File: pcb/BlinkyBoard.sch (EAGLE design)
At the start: 17 parts, among them Q1 16 MHz

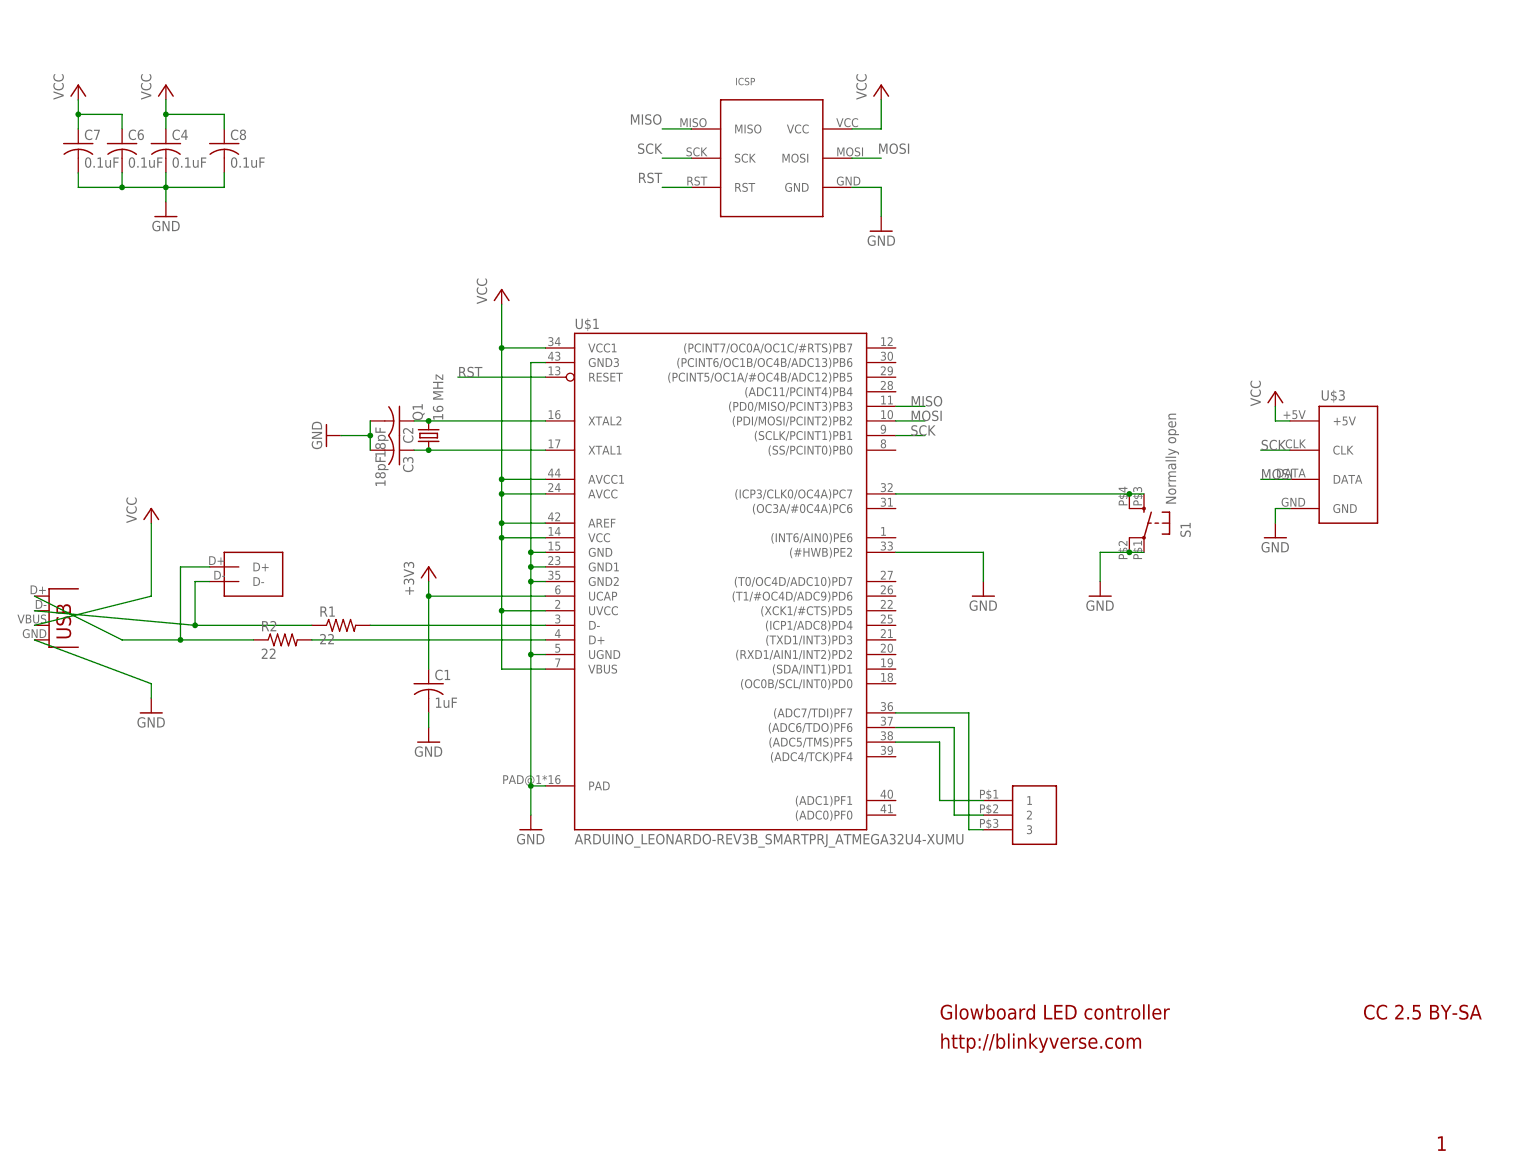
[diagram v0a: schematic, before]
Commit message: Switch to 2520 crystal, remove unused layers, rename components
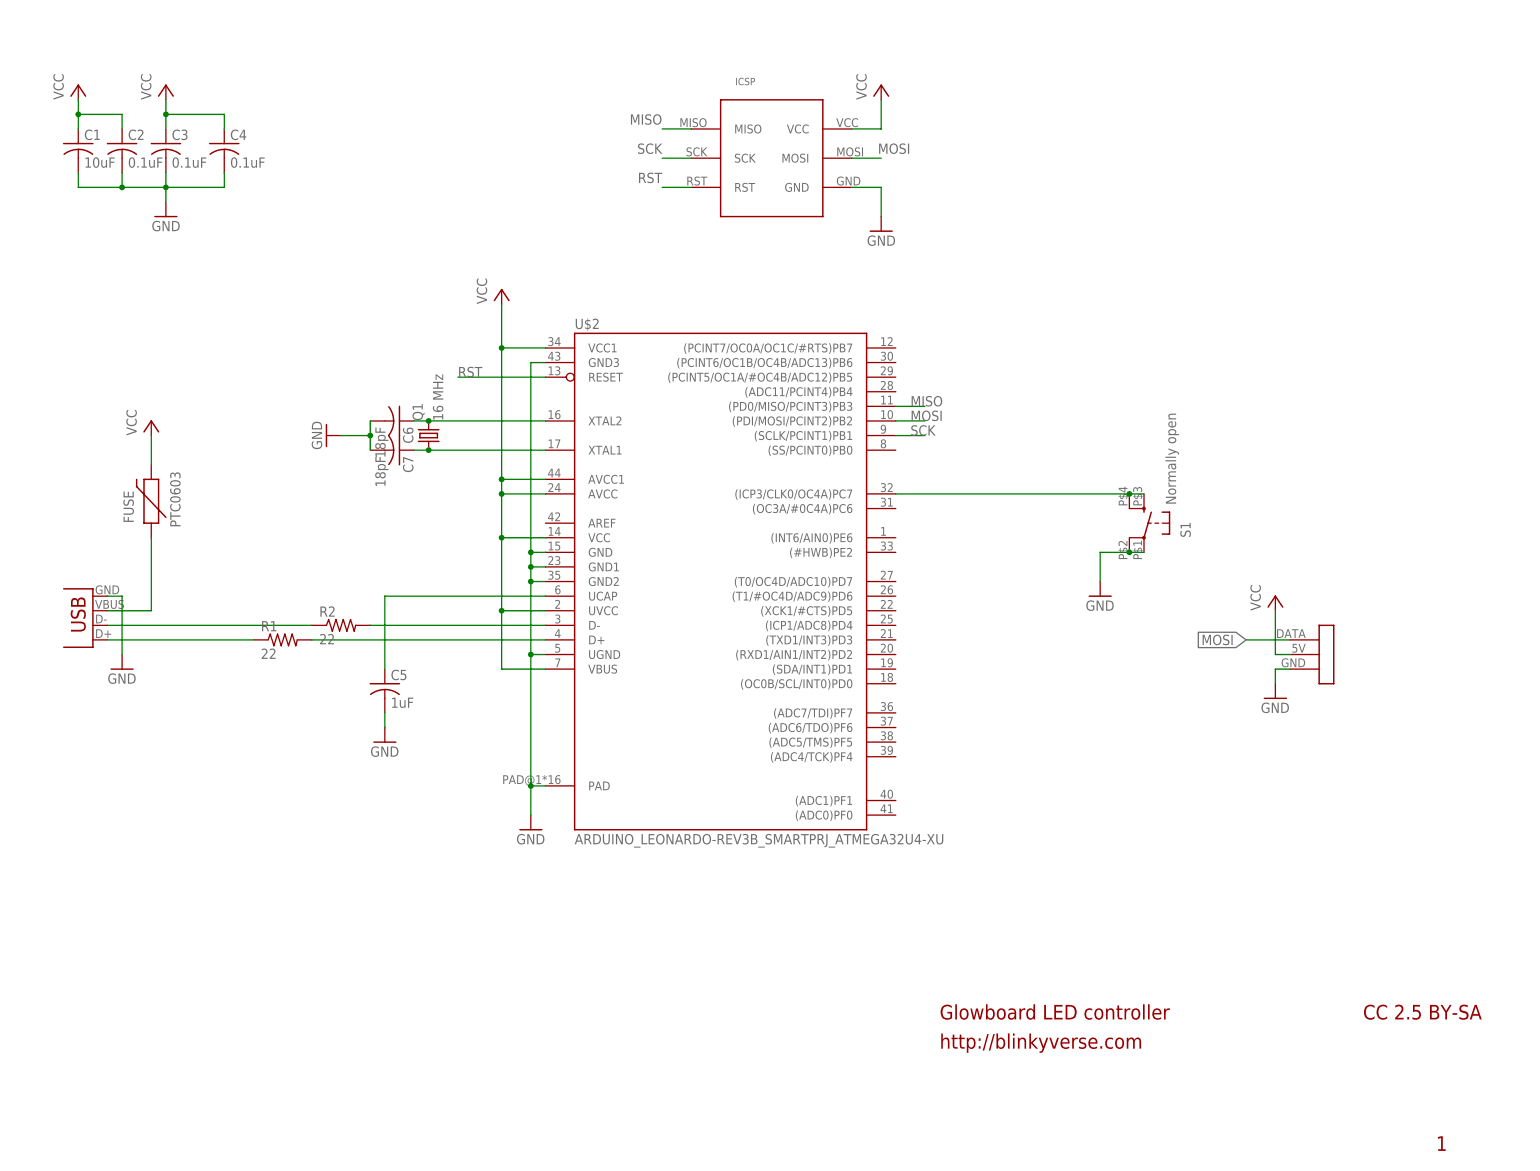
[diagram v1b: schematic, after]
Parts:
- removed C8: 0.1uF, adafruit:C-USC0603
- removed U$4: GLOWBOARD_ICSP, blinkyboard:GLOWBOARD_ICSP
- removed U$5: GLOWBOARD_EXPANSION_HEADER, blinkyboard:GLOWBOARD_EXPANSION_HEADER
- removed U$6: USB-MICROB, SparkFun:USB-MICROB
- added C5: 1uF, adafruit:C-USC0402
- added FUSE: PTC0603, SparkFun-PowerIC:PTC0603
- added WS1: WS2811_CONNECTOR, blinkiverse:WS2811_CONNECTOR
- C1: value 1uF -> 10uF; device adafruit:C-USC0603 -> adafruit:C-USC0402
- C2, C3: value 18pF -> 0.1uF; device adafruit:C-USC0603 -> adafruit:C-USC0402
- C4: device adafruit:C-USC0603 -> adafruit:C-USC0402
- C6, C7: value 0.1uF -> 18pF; device adafruit:C-USC0603 -> adafruit:C-USC0402
- Q1: device blinkiverse:CRYSTAL -> blinkiverse:CRYSTAL2520
- R1, R2: device adafruit:R-US_R0603 -> adafruit:R-US_R0402
- U$1: value ARDUINO_LEONARDO-REV3B_SMARTPRJ_ATMEGA32U4-XUMU -> USB-MICROB; device blinkiverse:ARDUINO_LEONARDO-REV3B_SMARTPRJ_ATMEGA32U4-XUMU -> SparkFun:USB-MICROB
- U$2: value GLOWBOARD_USB_TEST_PADS -> ARDUINO_LEONARDO-REV3B_SMARTPRJ_ATMEGA32U4-XU; device blinkyboard:GLOWBOARD_USB_TEST_PADS -> blinkiverse:ARDUINO_LEONARDO-REV3B_SMARTPRJ_ATMEGA32U4-XU
- U$3: value GLOWBOARD_PAD_CONNECTION -> GLOWBOARD_ICSP; device blinkyboard:GLOWBOARD_PAD_CONNECTION -> blinkyboard:GLOWBOARD_ICSP
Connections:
- removed net +3V3: C1.1, U$1.UCAP
- removed net N$6: U$1.(ADC6/TDO)PF6, U$5.2
- removed net N$7: U$1.(ADC7/TDI)PF7, U$5.3
- new net N$2: C5.1, U$2.UCAP
- net D+: now also R1.2, U$2.D+; no longer R2.2, U$1.D+
- net D+_IN: now also R1.1, U$1.D+; no longer R2.1, U$2.D+, U$6.D+
- net D-: now also R2.2, U$2.D-; no longer R1.2, U$1.D-
- net D-_IN: now also R2.1, U$1.D-; no longer R1.1, U$2.D-, U$6.D-
- net GND: now also C5.2, U$2.GND, U$2.GND1, U$2.GND2, U$2.GND3, U$2.PAD, U$2.UGND, WS1.GND; no longer C8.2, U$1.(#HWB)PE2, U$1.GND1, U$1.GND2, U$1.GND3, U$1.PAD, U$1.UGND, U$4.GND, U$6.GND
- net MISO: now also U$2.(PD0/MISO/PCINT3)PB3, U$3.MISO; no longer U$1.(PD0/MISO/PCINT3)PB3, U$4.MISO
- net MOSI: now also U$2.(PDI/MOSI/PCINT2)PB2, U$3.MOSI, WS1.DATA; no longer U$1.(PDI/MOSI/PCINT2)PB2, U$3.DATA, U$4.MOSI
- net N$1: now also FUSE.1, U$1.VBUS; no longer U$1.(ADC5/TMS)PF5, U$5.1
- net N$10: now also U$2.(ICP3/CLK0/OC4A)PC7; no longer U$1.(ICP3/CLK0/OC4A)PC7
- net N$8: now also C6.1, U$2.XTAL2; no longer C2.1, U$1.XTAL2
- net N$9: now also C7.1, U$2.XTAL1; no longer C3.1, U$1.XTAL1
- net RST: now also U$2.RESET, U$3.RST; no longer U$1.RESET, U$4.RST
- net SCK: now also U$2.(SCLK/PCINT1)PB1, U$3.SCK; no longer U$1.(SCLK/PCINT1)PB1, U$3.CLK, U$4.SCK
- net VCC: now also C1.1, C2.1, C3.1, FUSE.2, U$2.AVCC, U$2.AVCC1, U$2.UVCC, U$2.VBUS, U$2.VCC, U$2.VCC1, U$3.VCC, WS1.5V; no longer C6.1, C7.1, C8.1, U$1.AREF, U$1.AVCC, U$1.AVCC1, U$1.UVCC, U$1.VBUS, U$1.VCC, U$1.VCC1, U$3.+5V, U$4.VCC, U$6.VBUS
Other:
- moved on the sheet: C1, C2, C3, C4, C6, C7, R1, R2

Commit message: Update 0402 resistor, add ICSP pads as tiny headers, make board smaller
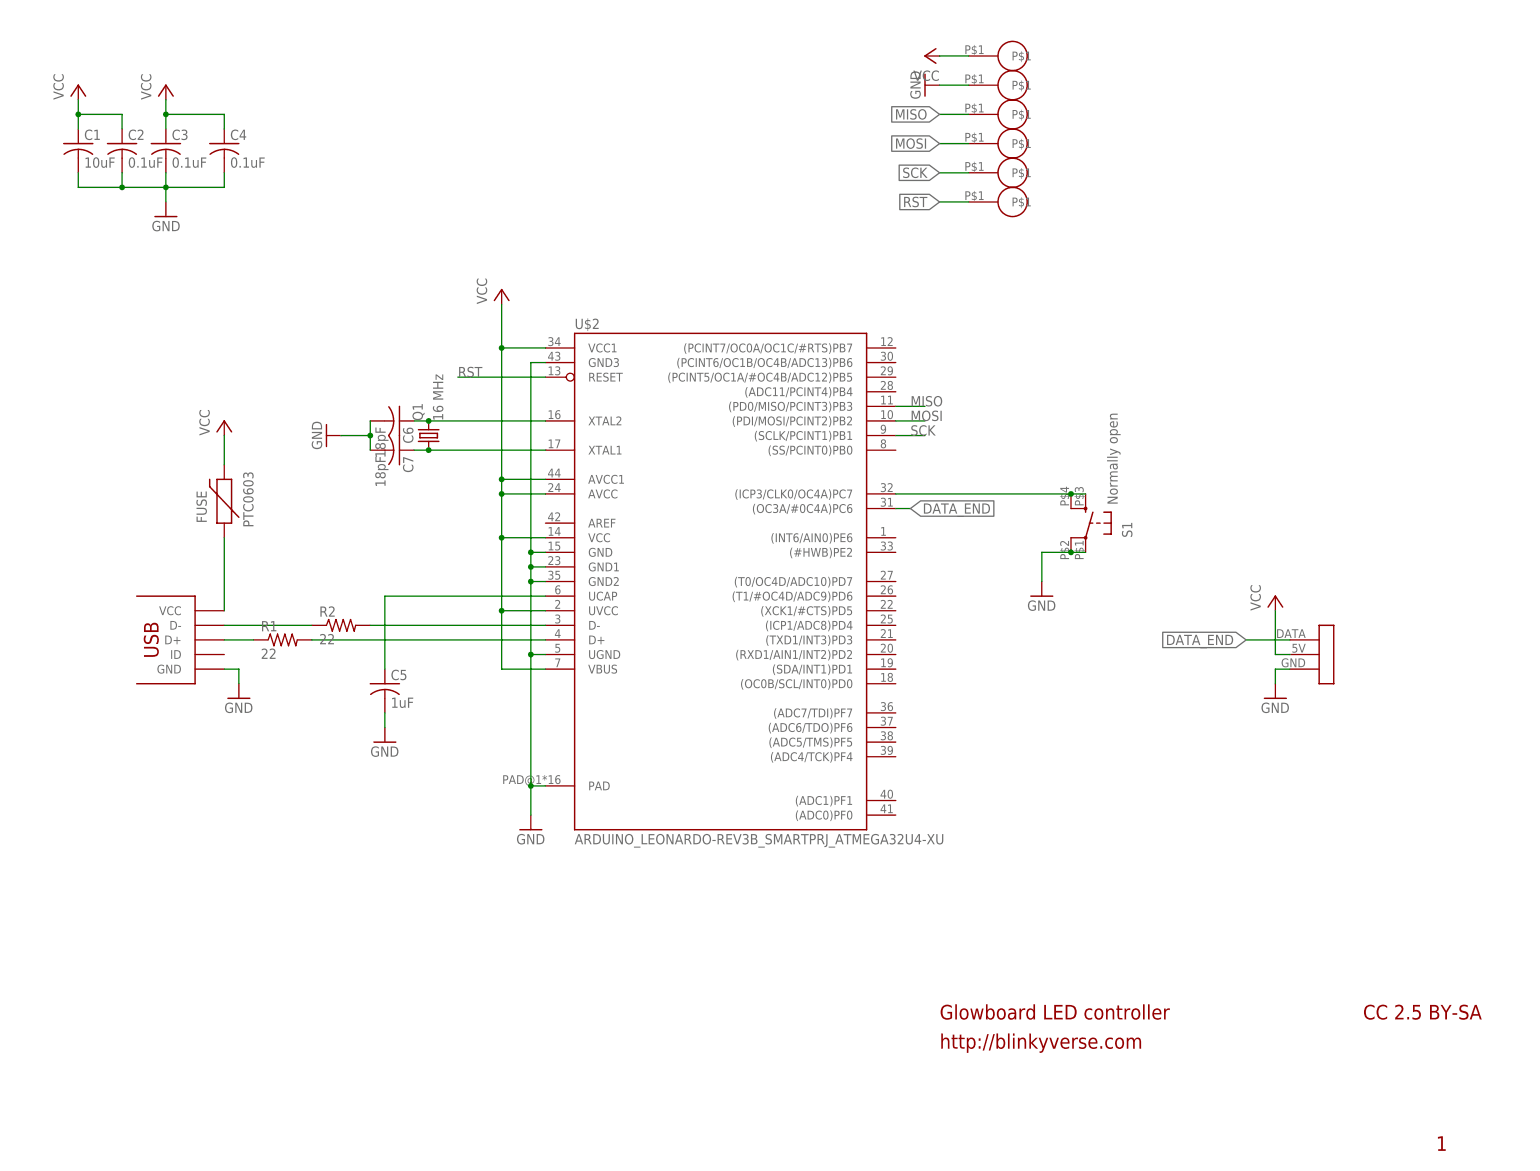
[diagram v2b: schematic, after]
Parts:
- added U$4: MICRO_USB, blinkiverse:MICRO_USB
- added U$5, U$6, U$7, U$8: TEST_VIA, blinkiverse:TEST_VIA
- C1, C2, C3, C4, C5, C6, C7: device adafruit:C-USC0402 -> blinkiverse:C_US
- R1, R2: device adafruit:R-US_R0402 -> blinkiverse:R_US
- U$1: value USB-MICROB -> TEST_VIA; device SparkFun:USB-MICROB -> blinkiverse:TEST_VIA
- U$3: value GLOWBOARD_ICSP -> TEST_VIA; device blinkyboard:GLOWBOARD_ICSP -> blinkiverse:TEST_VIA
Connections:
- new net DATA_END: U$2.(OC3A/#0C4A)PC6, WS1.DATA
- net D+_IN: now also U$4.D+; no longer U$1.D+
- net D-_IN: now also U$4.D-; no longer U$1.D-
- net GND: now also U$4.GND, U$7.P$1; no longer U$1.GND, U$3.GND
- net MISO: now also U$1.P$1; no longer U$3.MISO
- net MOSI: now also U$3.P$1; no longer U$3.MOSI, WS1.DATA
- net N$1: now also U$4.VCC; no longer U$1.VBUS
- net RST: now also U$6.P$1; no longer U$3.RST
- net SCK: now also U$5.P$1; no longer U$3.SCK
- net VCC: now also U$8.P$1; no longer U$3.VCC
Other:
- moved on the sheet: FUSE, S1
